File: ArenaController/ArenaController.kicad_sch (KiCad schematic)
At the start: 36 parts, among them J1 RJ45, J2 RJ45, J3 5Pin_5mm_plus_2.54_pin, J4 RJ45, J5 RJ45, J6 RJ45, J7 Barrel_Jack, Q1 IRLIZ44N, Q2 IRLIZ44N, Q3 IRLIZ44N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

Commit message: Update to shit.
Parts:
- removed U2: 20mmx50mm_buckboost, footprints:buckboost_mount, symbol symbols:20mmx50mm_buckboost
- added C1, C2: C, symbol Device:C
- added R14, R15: R_US, symbol Device:R_US
- added U2: TPS563200, Package_TO_SOT_SMD:SOT-23-6, symbol Regulator_Switching:TPS563200
- J1: Connection (none) -> Stacklight Red
- J2: Connection (none) -> Stacklight Blue
- J5: Connection (none) -> Team Blue
- J6: Connection (none) -> Team Red
- J7: footprint Connector_BarrelJack:BarrelJack_Horizontal -> footprints:BarrelJack_Horizontal_TwoPin
- Q1, Q2, Q3, Q4, Q5: footprint Package_TO_SOT_THT:TO-220F-3_Vertical -> Package_TO_SOT_THT:TO-220F-3_Horizontal_TabDown
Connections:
- net +12V: now also C1.1
- net GND: now also R15.1, U2.1 (GND)
- new net: C2.2, U2.6 (VBST)
- new net: R14.1, R15.2, U2.4 (VFB)
- new net: C1.2, U2.3 (VIN), U2.5 (EN)
- new net +3.3V: R14.2
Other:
- note added: "12V to 3.3V DC DC What the fuck is this thing?"
- note added: "Microcontroller"
- note added: "TODO: Replace ESP32 Devkit 1 w/ ESP32 Devkit 4 (as that's what I've got on hand.) Replace LEDs with smaller diameter ones? Standardize mounting footprint. Add 12v to 5v schematic that's not dogshit! Add RS485 connection."
- note removed: "12V to 5V DC DC"
- note removed: "Microcontroller (Box Brain)"

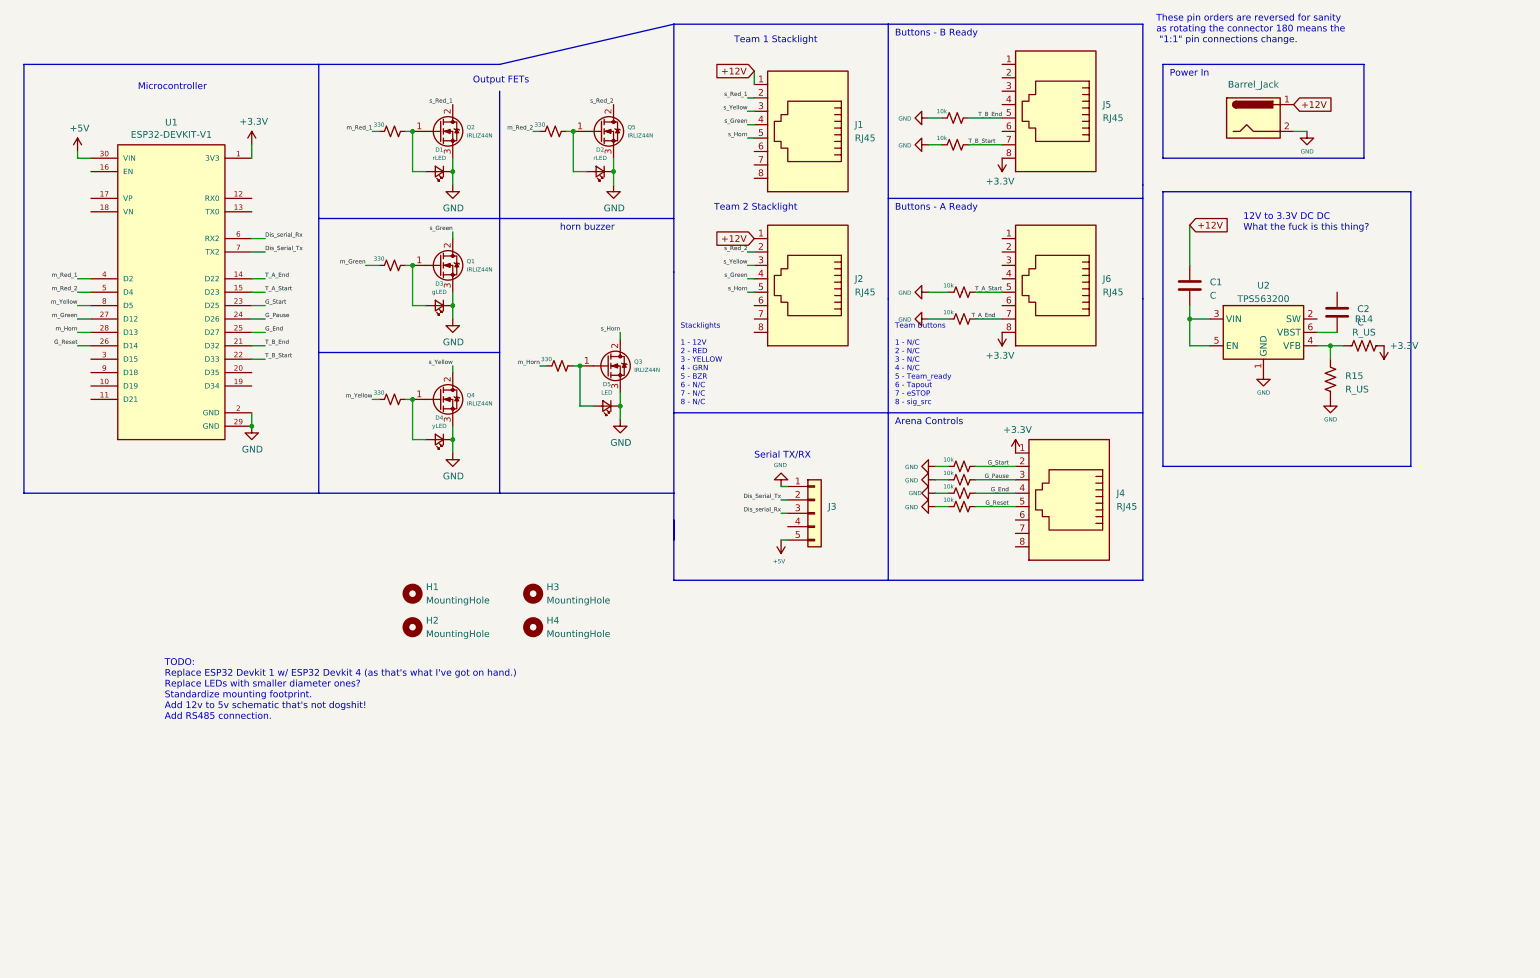
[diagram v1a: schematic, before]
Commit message: Add microswitch for start buttons.
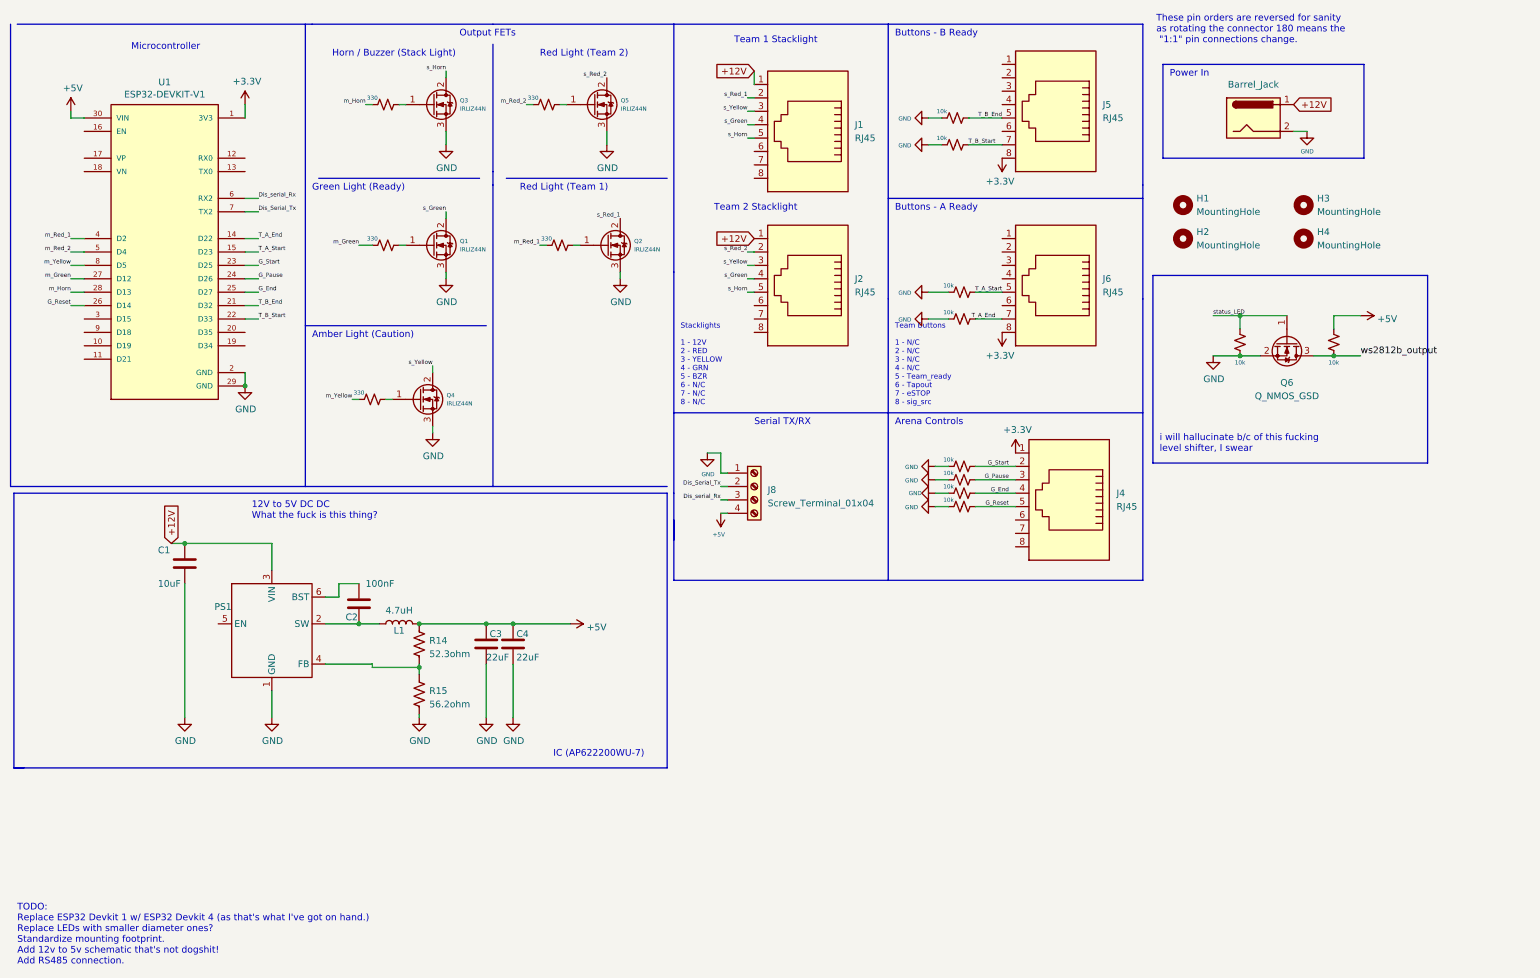
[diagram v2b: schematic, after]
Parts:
- removed D1, D2: rLED, LED_THT:LED_D10.0mm, symbol Device:LED_Small
- removed D3: gLED, LED_THT:LED_D10.0mm, symbol Device:LED_Small
- removed D4: yLED, LED_THT:LED_D10.0mm, symbol Device:LED_Small
- removed D5: LED, LED_THT:LED_D10.0mm, symbol Device:LED_Small
- removed J3: 5Pin_5mm_plus_2.54_pin, footprints:5pin_5mmpitch_plus_2.54_combo, symbol symbols:5Pin_5mm_plus_2.54_pin
- removed U2: TPS563200, Package_TO_SOT_SMD:SOT-23-6, symbol Regulator_Switching:TPS563200
- added C3, C4: 22uF, symbol Device:C
- added J8: Screw_Terminal_01x04, TerminalBlock_MetzConnect:TerminalBlock_MetzConnect_Type011_RT05504HBWC_1x04_P5.00mm_Horizontal, symbol Connector:Screw_Terminal_01x04
- added L1: 4.7uH, symbol Device:L
- added PS1: ~, Package_TO_SOT_SMD:TSOT-23-6_HandSoldering, symbol symbols:AP62200
- added Q6: Q_NMOS_GSD, symbol Device:Q_NMOS_GSD
- added R16, R17: 10k, Resistor_THT:R_Axial_DIN0207_L6.3mm_D2.5mm_P10.16mm_Horizontal, symbol Device:R_Small_US
- C1: value C -> 10uF
- C2: value C -> 100nF
- R14: value R_US -> 52.3ohm
- R15: value R_US -> 56.2ohm
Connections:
- net +12V: now also C1.2, PS1.3 (VIN); no longer C1.1
- net +5V: now also R14.1, C3.2, C4.2, J8.4 (Pin_4), L1.2, R17.1
- net Dis_Serial_Tx: now also J8.2 (Pin_2)
- net Dis_serial_Rx: now also J8.3 (Pin_3)
- net GND: now also C1.1, R15.2, C3.1, C4.1, J8.1 (Pin_1), PS1.1 (GND), Q6.2 (S), R16.2; no longer R15.1
- net at C2.1: now also L1.1, PS1.2 (SW)
- net at C2.2: now also PS1.6 (BST)
- net +3.3V: no longer names the net of R14.2
- net +3.3V: now also R15.1, PS1.4 (FB)
- new net status_LED: Q6.1 (G), R16.1
- new net ws2812b_output: Q6.3 (D), R17.2
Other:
- note added: "12V to 5V DC DC What the fuck is this thing?"
- note added: "Amber Light (Caution)"
- note added: "Green Light (Ready)"
- note added: "Horn / Buzzer (Stack Light)"
- note added: "IC (AP622200WU-7)"
- note added: "Red Light (Team 1)"
- note added: "Red Light (Team 2)"
- note added: "i will hallucinate b/c of this fucking level shifter, I swear"
- note removed: "12V to 3.3V DC DC What the fuck is this thing?"
- note removed: "horn buzzer"
- moved on the sheet: H1, H2, H3, H4, Q1, Q2, Q3, Q4, Q5, U1

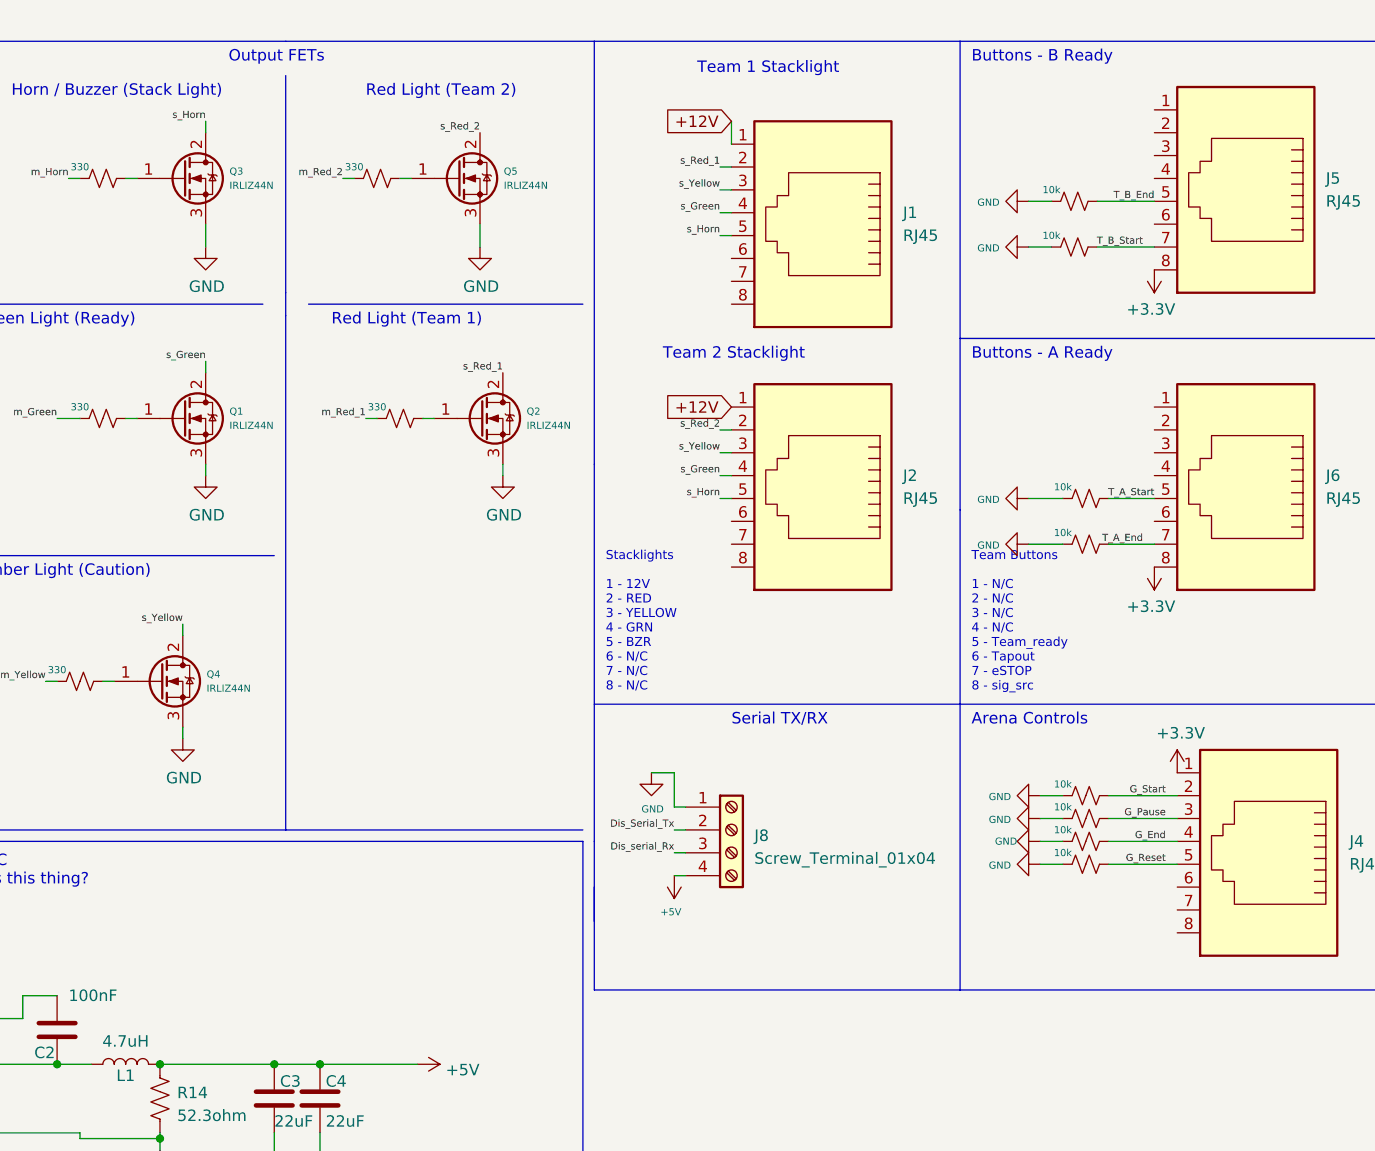
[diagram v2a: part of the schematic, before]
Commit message: Added new files, swap to new FET for toggling, added FET as symbols.
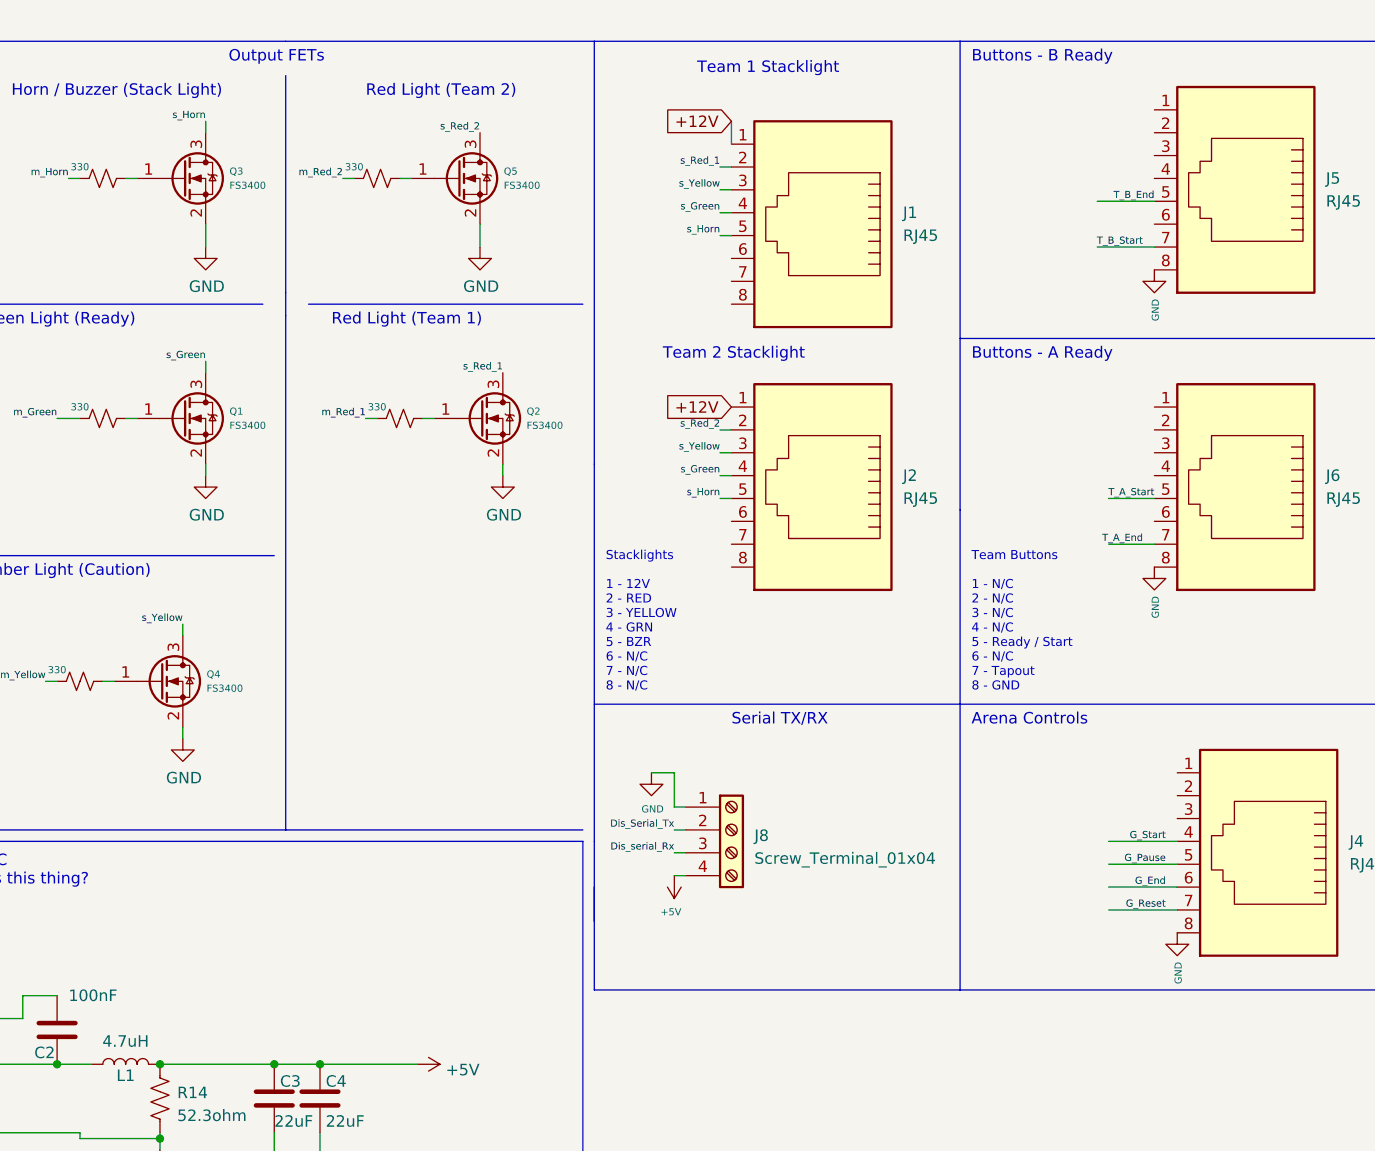
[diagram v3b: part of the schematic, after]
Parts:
- removed R1, R10, R11, R12, R13, R7, R8, R9: 10k, Resistor_THT:R_Axial_DIN0207_L6.3mm_D2.5mm_P10.16mm_Horizontal, symbol Device:R_Small_US
- Q1, Q2, Q3, Q4, Q5: value IRLIZ44N -> FS3400; footprint Package_TO_SOT_THT:TO-220F-3_Horizontal_TabDown -> Package_TO_SOT_SMD:SOT-23; symbol Transistor_FET:IRLIZ44N -> symbols:FS3400
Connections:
- net +3V3: no longer J4.1, J5.8, J6.8
- net GND: now also J4.8, J5.8, J6.8, Q1.2 (S), Q2.2 (S), Q3.2 (S), Q4.2 (S), Q5.2 (S); no longer Q1.3 (S), Q2.3 (S), Q3.3 (S), Q4.3 (S), Q5.3 (S)
- net G_End: now also J4.6; no longer J4.4
- net G_Pause: now also J4.5; no longer J4.3
- net G_Reset: now also J4.7; no longer J4.5
- net G_Start: now also J4.4; no longer J4.2
- net s_Green: now also Q1.3 (D); no longer Q1.2 (D)
- net s_Horn: now also Q3.3 (D); no longer Q3.2 (D)
- net s_Red_1: now also Q2.3 (D); no longer Q2.2 (D)
- net s_Red_2: now also Q5.3 (D); no longer Q5.2 (D)
- net s_Yellow: now also Q4.3 (D); no longer Q4.2 (D)
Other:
- note added: "Team Buttons 1 - N/C 2 - N/C 3 - N/C 4 - N/C 5 - Ready / Start 6 - N/C 7 - Tapout 8 - GND"
- note removed: "Team Buttons 1 - N/C 2 - N/C 3 - N/C 4 - N/C 5 - Team_ready 6 - Tapout 7 - eSTOP 8 - sig_src"
